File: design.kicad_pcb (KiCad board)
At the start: 2 copper layers, 25 x 22.9 mm, 14 parts, among them J1 Conn_01x02, J2 Conn_01x02, J3 Conn_01x03, J4 Conn_01x03, U1 TPS61099YFFT

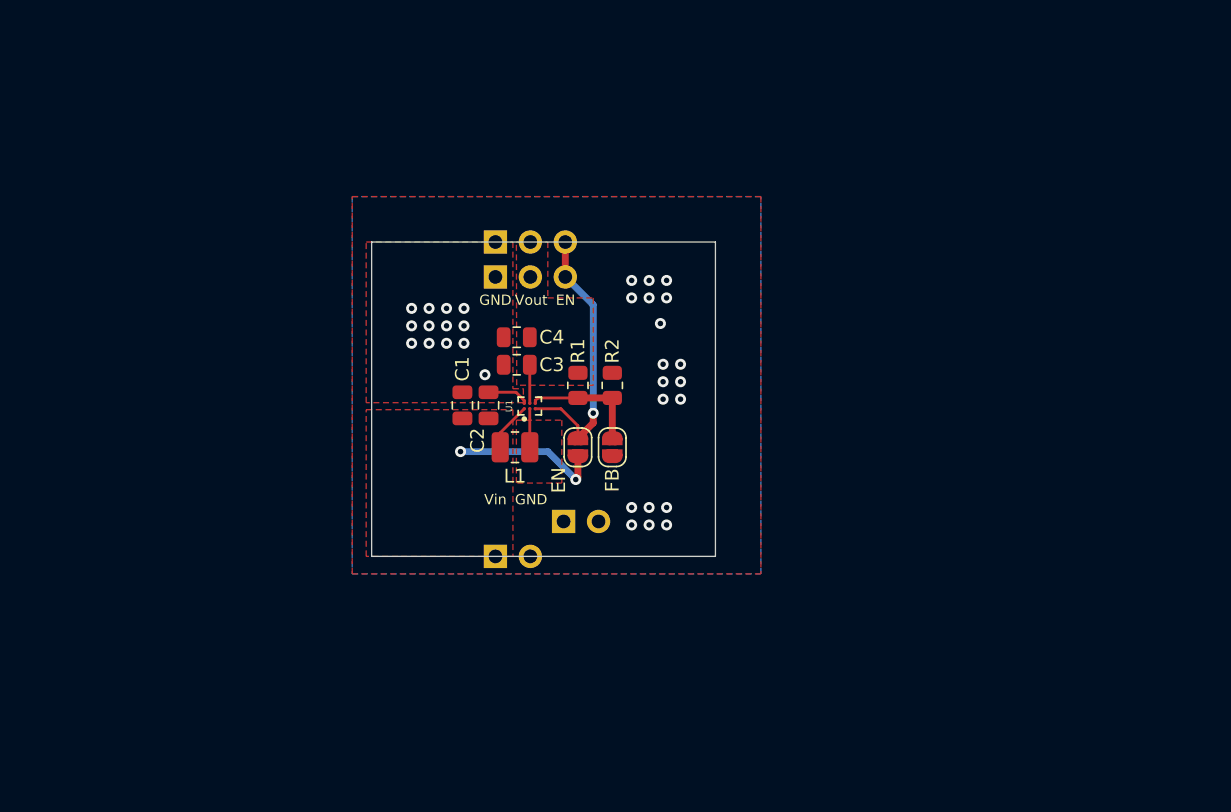
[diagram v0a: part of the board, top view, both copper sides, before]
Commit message: Delete all template stuff
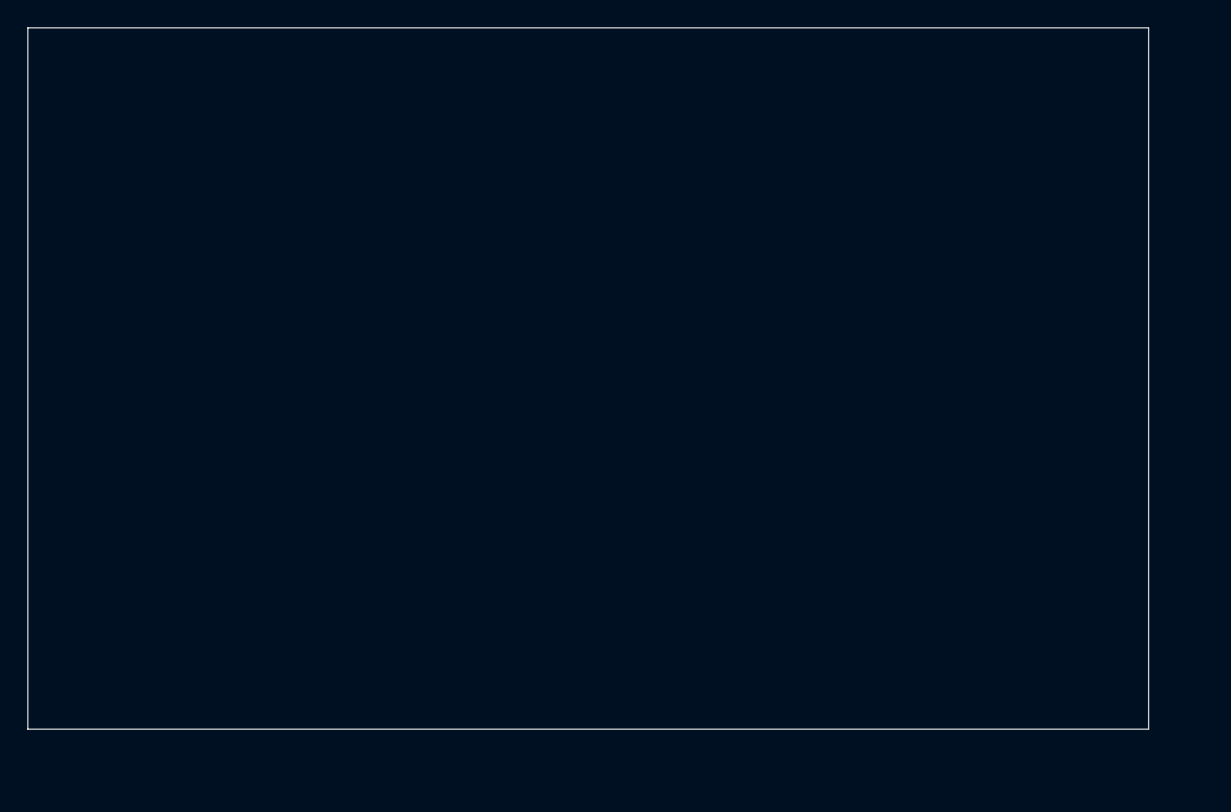
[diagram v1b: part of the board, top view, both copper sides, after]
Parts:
- removed C1, C2, C3, C4: C_Small, Capacitor_SMD:C_0805_2012Metric
- removed J1, J2: Conn_01x02, Connector_PinHeader_2.54mm:PinHeader_1x02_P2.54mm_Vertical
- removed J3, J4: Conn_01x03, Connector_PinHeader_2.54mm:PinHeader_1x03_P2.54mm_Vertical
- removed JP1, JP2: SolderJumper_2_Open, Jumper:SolderJumper-2_P1.3mm_Open_RoundedPad1.0x1.5mm
- removed L1: L_Small, Inductor_SMD:L_1008_2520Metric
- removed R1, R2: R_Small, Resistor_SMD:R_0805_2012Metric
- removed U1: TPS61099YFFT, Converter_DCDC_custom:BGA6N40P3X2_122X88X62N
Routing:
- net En: track 19.9 -> 0.00 mm, vias 1 -> 0
- net Vin: track 14.5 -> 0.00 mm, vias 2 -> 0
- net FB: track 8.82 -> 0.00 mm
- net GND: track 3.05 -> 0.00 mm, vias 32 -> 0
- net Vout: track 2.80 -> 0.00 mm
- net SW: track 2.80 -> 0.00 mm
- removed copper zone on B.Cu, net GND
- removed copper zone on F.Cu, net GND
- removed copper zone on F.Cu, net SW
- removed copper zone on F.Cu, net Vin
- removed copper zone on F.Cu, net Vout
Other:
- board size 25 x 22.9 mm -> 81.5 x 51 mm
- board text removed: "EN"
- board text removed: "GND"
- board text removed: "Vin"
- board text removed: "Vout"

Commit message: Update design.kicad_pcb
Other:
- board text added: "sdfs"
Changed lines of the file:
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@@
   (net 0 "")
   (gr_rect (start 109 68.5) (end 190.5 119.5) (layer "Edge.Cuts") (width 0.05) (fill none))
+  (gr_text "sdfs" (at 162 102.5) (layer "F.SilkS")
+    (effects (font (size 1 1) (thickness 0.15)))
+  )
   (gr_text "<<project_name>>\n<<ID>>\n<<version>>\n<<date>>\n<<hash>>\n<<website_link>>" (at 229.1 153) (layer "F.SilkS")
     (effects (font (size 1 1) (thickness 0.15)))

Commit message: Update design.kicad_pcb
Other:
- board text added: "sdfs dkajölskdj"
- board text removed: "sdfs"
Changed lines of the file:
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@@
   (net 0 "")
   (gr_rect (start 109 68.5) (end 190.5 119.5) (layer "Edge.Cuts") (width 0.05) (fill none))
-  (gr_text "sdfs" (at 162 102.5) (layer "F.SilkS")
+  (gr_text "sdfs\n\ndkajölskdj" (at 162 102.5) (layer "F.SilkS")
     (effects (font (size 1 1) (thickness 0.15)))
   )
